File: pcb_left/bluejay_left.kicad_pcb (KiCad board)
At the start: 2 copper layers, 147 x 140.5 mm, 82 parts, among them J1 SJ-43514, U1 ATmega328P-PU, Y1 16MHz

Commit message: remove mounting hole 9
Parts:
- removed H9: M2, MountingHole:MountingHole_2.2mm_M2_Pad
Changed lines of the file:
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@@
     )
-  )
-  (footprint "MountingHole:MountingHole_2.2mm_M2_Pad" (layer "F.Cu")
-    (at 56.95 64.15)
-    (descr "Mounting Hole 2.2mm, M2")
-    (tags "mounting hole 2.2mm m2")
-    (property "Sheetfile" "bluejay_left.kicad_sch")
-    (property "Sheetname" "")
-    (property "exclude_from_bom" "")
-    (attr exclude_from_pos_files exclude_from_bom)
-    (fp_text reference "H9" (at 0 -3.2) (layer "F.SilkS") hide
-      (effects (font (size 1 1) (thickness 0.15)))
-    )
-    (fp_text value "M2" (at 0 3.2) (layer "F.Fab")
-      (effects (font (size 1 1) (thickness 0.15)))
-    )
-    (fp_text user "${REFERENCE}" (at 0 0) (layer "F.Fab")
-      (effects (font (size 1 1) (thickness 0.15)))
-    )
-    (fp_circle (center 0 0) (end 2.2 0) (layer "Cmts.User") (width 0.15) (fill none))
-    (fp_circle (center 0 0) (end 2.45 0) (layer "F.CrtYd") (width 0.05) (fill none))
-    (pad "1" thru_hole circle (at 0 0) (size 4.4 4.4) (drill 2.2) (layers *.Cu *.Mask))
   )
   (footprint "BlueJay footprints:SW_MX_Plate" (layer "F.Cu")

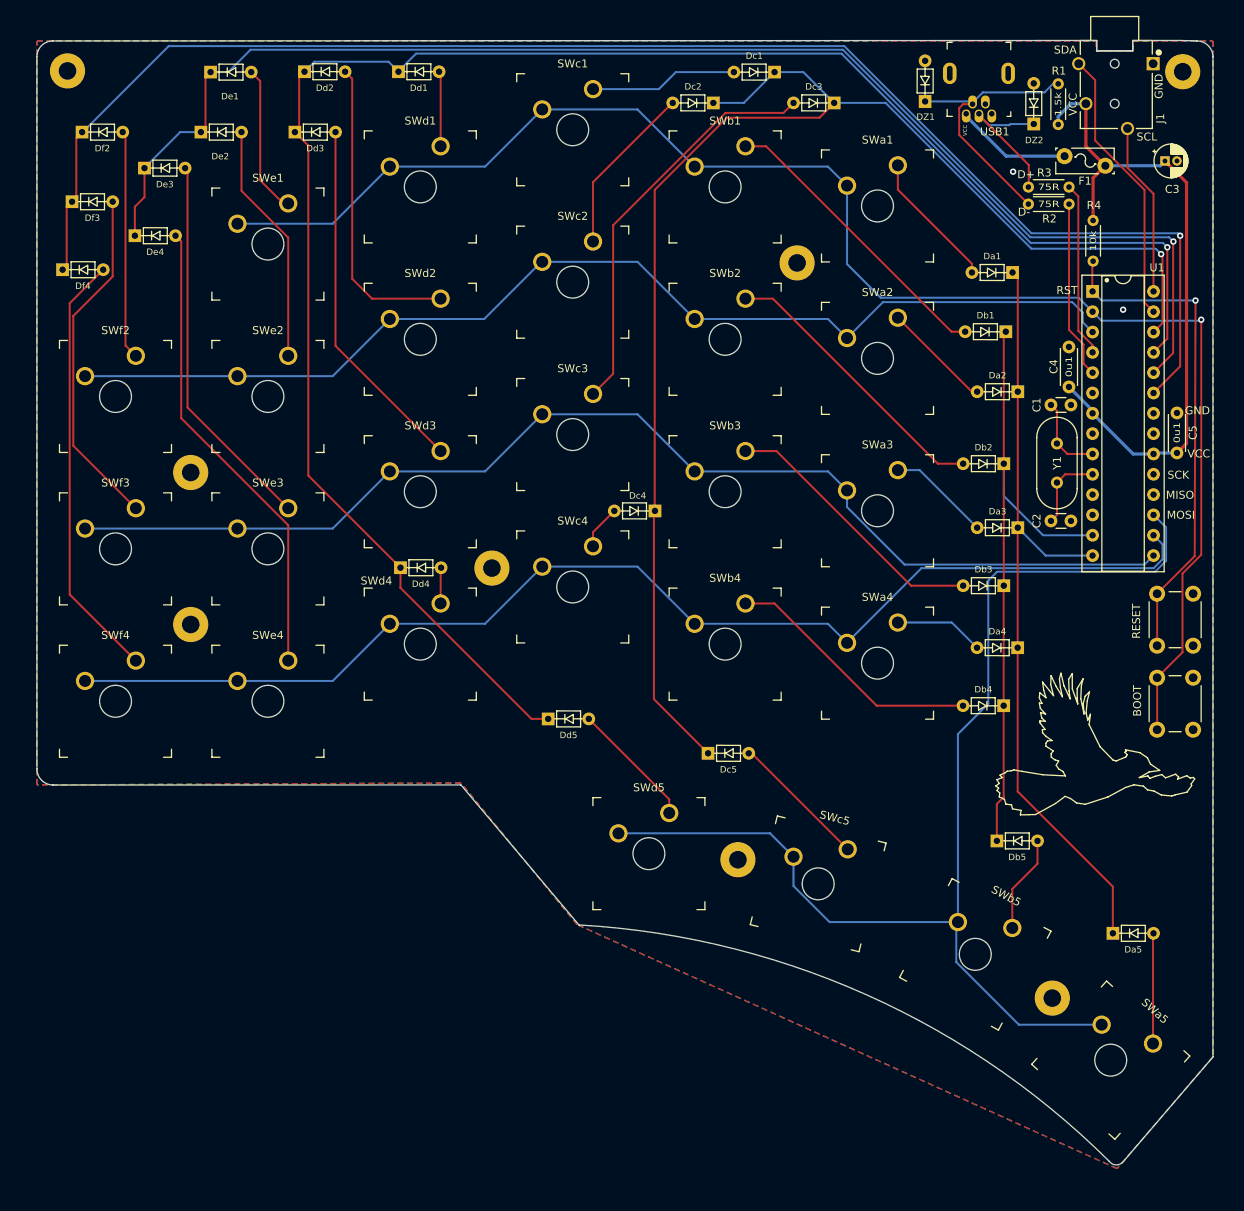
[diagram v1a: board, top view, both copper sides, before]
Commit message: Round edges of PCB
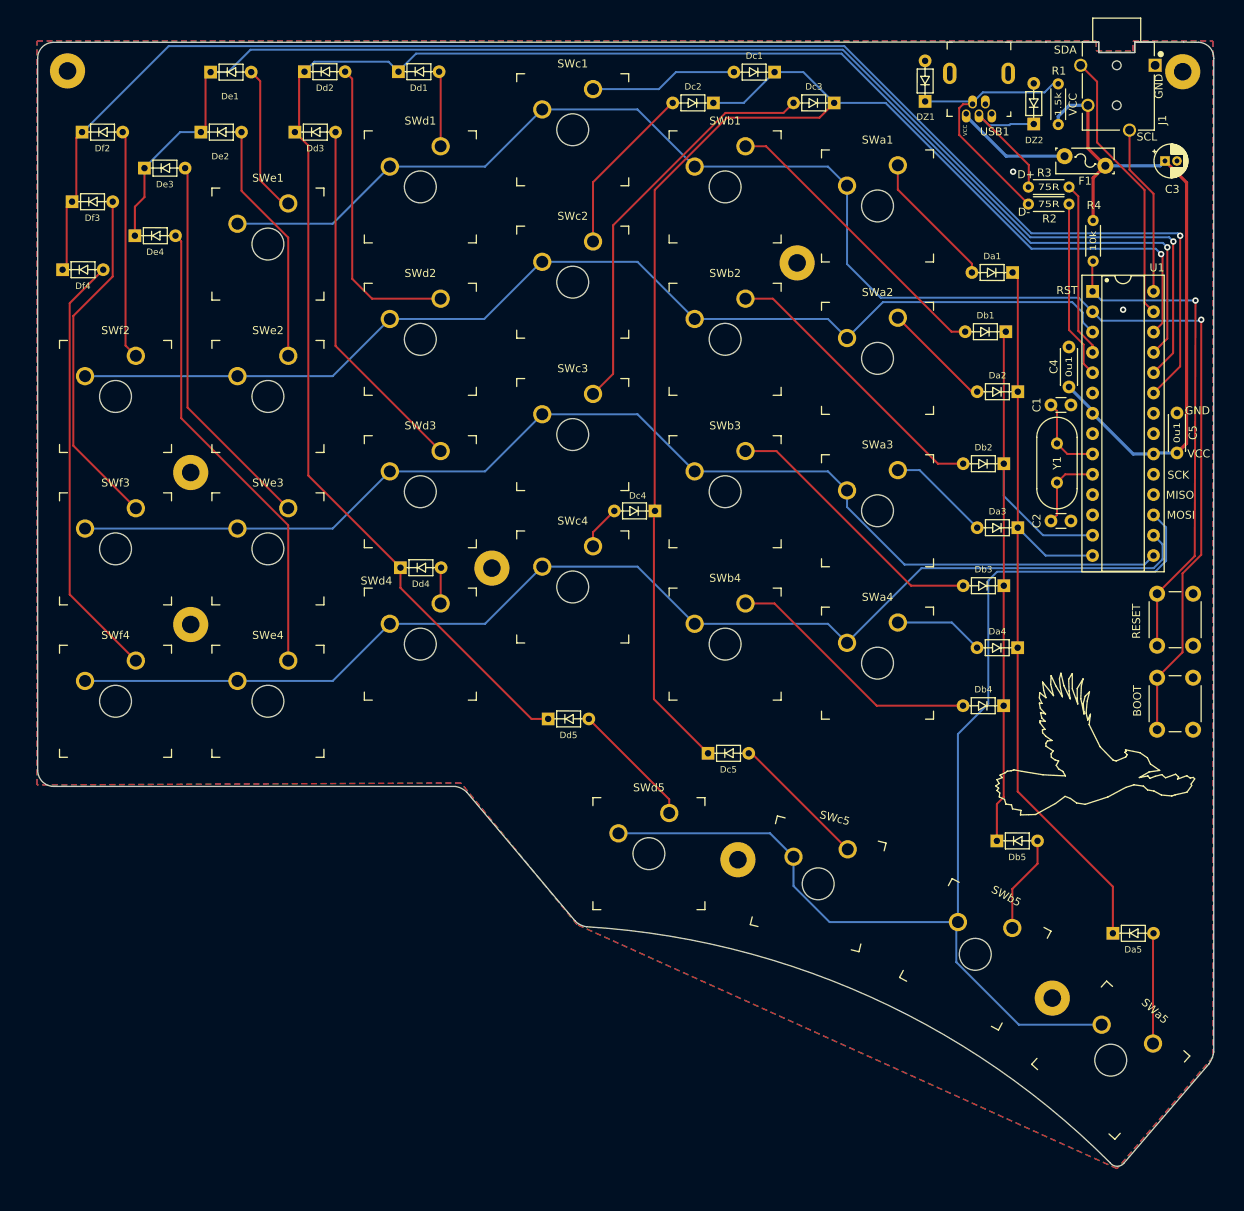
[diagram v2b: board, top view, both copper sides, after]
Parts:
- moved J1 0.32 mm to (49.0, -50.7)
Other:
- outline, holes or cut-outs redrawn
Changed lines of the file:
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@@
   )
   (footprint "BlueJay footprints:CUI_SJ-43514" (layer "F.Cu")
-    (at 48.7 -50.9 -90)
+    (at 48.95 -50.7 -90)
     (property "Field4" "MANUFACTURER RECOMMENDATIONS")
     (property "Field5" "CUI INC")
@@
   (gr_line locked (start 26.028999 -42.674998) (end 26.028999 -42.674998) (layer "Eco1.User") (width 0.188976))
   (gr_line locked (start -16.546013 52.286989) (end -16.546013 38.286989) (layer "Eco1.User") (width 0.188976))
-  (gr_line (start 60.9812 70.6563) (end 49.7812 83.7263) (layer "Edge.Cuts") (width 0.1))
-  (gr_arc (start -18.2688 54.1563) (mid 17.583107 62.841492) (end 48.0112 83.6963) (layer "Edge.Cuts") (width 0.1))
-  (gr_arc (start 58.9812 -56.3437) (mid 60.393459 -55.755959) (end 60.981199 -54.3437) (layer "Edge.Cuts") (width 0.1))
-  (gr_line (start 60.9812 70.6563) (end 60.981199 -54.3437) (layer "Edge.Cuts") (width 0.1))
-  (gr_arc (start -86.024489 -54.35145) (mid -85.442713 -55.767431) (end -84.024489 -56.3437) (layer "Edge.Cuts") (width 0.1))
-  (gr_arc (start -84.02552 36.663017) (mid -85.443204 36.061839) (end -86.025519 34.6363) (layer "Edge.Cuts") (width 0.1))
-  (gr_line (start -86.024489 -54.35145) (end -86.025519 34.6363) (layer "Edge.Cuts") (width 0.1))
-  (gr_line (start -84.02552 36.663017) (end -33.0188 36.6563) (layer "Edge.Cuts") (width 0.1))
-  (gr_line (start -33.0188 36.6563) (end -18.2688 54.1563) (layer "Edge.Cuts") (width 0.1))
-  (gr_line (start 58.9812 -56.3437) (end 57.05 -56.4) (layer "Edge.Cuts") (width 0.1))
-  (gr_line (start 39.85 -56.4) (end -84.024489 -56.3437) (layer "Edge.Cuts") (width 0.1))
-  (gr_arc (start 49.7812 83.7263) (mid 48.888799 84.147698) (end 48.0112 83.6963) (layer "Edge.Cuts") (width 0.1))
+  (gr_line (start 60.48 71.53) (end 49.88 83.9) (layer "Edge.Cuts") (width 0.1))
+  (gr_arc (start -17.32 54.38) (mid 18.101214 63.120674) (end 48.11 83.87) (layer "Edge.Cuts") (width 0.1))
+  (gr_arc (start 59.2 -56.175) (mid 60.553201 -55.55994) (end 61.08 -54.17) (layer "Edge.Cuts") (width 0.1))
+  (gr_line (start 61.08 70.05) (end 61.08 -54.17) (layer "Edge.Cuts") (width 0.1))
+  (gr_arc (start -85.93 -54.18) (mid -85.347749 -55.594848) (end -83.93 -56.17) (layer "Edge.Cuts") (width 0.1))
+  (gr_arc (start -83.93 36.84) (mid -85.348353 36.23717) (end -85.93 34.81) (layer "Edge.Cuts") (width 0.1))
+  (gr_line (start -85.93 -54.18) (end -85.93 34.81) (layer "Edge.Cuts") (width 0.1))
+  (gr_line (start -83.93 36.84) (end -33.72 36.84) (layer "Edge.Cuts") (width 0.1))
+  (gr_line (start -32.31 37.54) (end -18.73 53.68) (layer "Edge.Cuts") (width 0.1))
+  (gr_line (start 59.2 -56.175) (end 57.3 -56.2) (layer "Edge.Cuts") (width 0.1))
+  (gr_arc (start -17.32 54.38) (mid -18.079496 54.13977) (end -18.73 53.68) (layer "Edge.Cuts") (width 0.1))
+  (gr_arc (start 61.08 70.05) (mid 60.863331 70.823783) (end 60.48 71.53) (layer "Edge.Cuts") (width 0.1))
+  (gr_line (start 40.1 -56.2) (end -83.93 -56.17) (layer "Edge.Cuts") (width 0.1))
+  (gr_arc (start 49.88 83.9) (mid 48.987603 84.321434) (end 48.11 83.87) (layer "Edge.Cuts") (width 0.1))
+  (gr_arc (start -33.72 36.84) (mid -32.960504 37.08023) (end -32.31 37.54) (layer "Edge.Cuts") (width 0.1))
   (gr_text "JLCJLCJLCJLC" (at -80.15 35.09) (layer "B.SilkS")
     (effects (font (size 1 1) (thickness 0.15)) (justify mirror))
@@
   (segment (start 41.4812 -1.1437) (end 41.4812 2.9063) (width 0.25) (layer "F.Cu") (net 3))
   (segment (start 42.515 -2.1775) (end 45.9312 -2.1775) (width 0.25) (layer "F.Cu") (net 3))
-  (segment (start 45.1 -43.1749) (end 45.1 -48.5) (width 0.4) (layer "F.Cu") (net 4))
   (segment (start 57.680711 -38.644189) (end 57.680711 -6.043211) (width 0.4) (layer "F.Cu") (net 4))
   (segment (start 54.9812 -41.3437) (end 57.680711 -38.644189) (width 0.4) (layer "F.Cu") (net 4))
+  (segment (start 45.35 -42.9249) (end 45.35 -48.25) (width 0.4) (layer "F.Cu") (net 4))
   (segment (start 57.680711 -6.043211) (end 56.4812 -4.8437) (width 0.4) (layer "F.Cu") (net 4))
   (segment (start 46 -39.2125) (end 46 -33.9) (width 0.4) (layer "F.Cu") (net 4))
   (segment (start 47.5312 -40.7437) (end 46 -39.2125) (width 0.4) (layer "F.Cu") (net 4))
-  (segment (start 47.5312 -40.7437) (end 45.1 -43.1749) (width 0.4) (layer "F.Cu") (net 4))
+  (segment (start 47.5312 -40.7437) (end 45.35 -42.9249) (width 0.4) (layer "F.Cu") (net 4))
   (segment (start 56.4812 -4.8437) (end 53.6774 -4.8437) (width 0.4) (layer "B.Cu") (net 4))
   (segment (start 54.3812 -40.7437) (end 54.9812 -41.3437) (width 0.4) (layer "B.Cu") (net 4))
   (segment (start 53.6774 -4.8437) (end 53.5512 -4.7175) (width 0.4) (layer "B.Cu") (net 4))
   (segment (start 47.5312 -40.7437) (end 54.3812 -40.7437) (width 0.4) (layer "B.Cu") (net 4))
-  (segment (start 43.23 -48.5) (end 41.64 -46.91) (width 0.4) (layer "B.Cu") (net 4))
+  (segment (start 45.35 -48.3) (end 43.03 -48.3) (width 0.4) (layer "B.Cu") (net 4))
+  (segment (start 41.64 -46.91) (end 41.64 -45.9) (width 0.4) (layer "B.Cu") (net 4))
+  (segment (start 43.03 -48.3) (end 41.64 -46.91) (width 0.4) (layer "B.Cu") (net 4))
   (segment (start 51.0112 -4.7175) (end 45.9312 -9.7975) (width 0.4) (layer "B.Cu") (net 4))
   (segment (start 45.9312 -10.1437) (end 42.9812 -13.0937) (width 0.4) (layer "B.Cu") (net 4))
-  (segment (start 45.1 -48.5) (end 43.23 -48.5) (width 0.4) (layer "B.Cu") (net 4))
   (segment (start 45.9312 -9.7975) (end 45.9312 -10.1437) (width 0.4) (layer "B.Cu") (net 4))
-  (segment (start 41.64 -46.91) (end 41.64 -45.9) (width 0.4) (layer "B.Cu") (net 4))
   (segment (start 53.5512 -4.7175) (end 51.0112 -4.7175) (width 0.4) (layer "B.Cu") (net 4))
   (segment (start 36.5863 -26.7437) (end 35.93 -27.4) (width 0.25) (layer "F.Cu") (net 5))
@@
   (segment (start 35.138376 -41.9437) (end 42.4312 -41.9437) (width 0.4) (layer "B.Cu") (net 40))
   (segment (start 30.1312 -46.950876) (end 35.138376 -41.9437) (width 0.4) (layer "B.Cu") (net 40))
-  (segment (start 50.3 -45.4) (end 50.3 -40.490832) (width 0.25) (layer "F.Cu") (net 41))
+  (segment (start 50.55 -45.15) (end 50.55 -40.240832) (width 0.25) (layer "F.Cu") (net 41))
   (segment (start 53.5512 -37.239632) (end 53.5512 -25.0375) (width 0.25) (layer "F.Cu") (net 41))
-  (segment (start 50.3 -40.490832) (end 53.5512 -37.239632) (width 0.25) (layer "F.Cu") (net 41))
-  (segment (start 44.2 -53.5) (end 46.249511 -51.450489) (width 0.25) (layer "F.Cu") (net 42))
-  (segment (start 46.249511 -51.450489) (end 46.249511 -43.905603) (width 0.25) (layer "F.Cu") (net 42))
+  (segment (start 50.55 -40.240832) (end 53.5512 -37.239632) (width 0.25) (layer "F.Cu") (net 41))
+  (segment (start 44.45 -53.3) (end 46.499511 -51.250489) (width 0.25) (layer "F.Cu") (net 42))
+  (segment (start 46.499511 -51.250489) (end 46.499511 -43.655603) (width 0.25) (layer "F.Cu") (net 42))
+  (segment (start 46.499511 -43.655603) (end 52.426689 -37.728425) (width 0.25) (layer "F.Cu") (net 42))
   (segment (start 52.426689 -37.728425) (end 52.426689 -23.622011) (width 0.25) (layer "F.Cu") (net 42))
-  (segment (start 46.249511 -43.905603) (end 52.426689 -37.728425) (width 0.25) (layer "F.Cu") (net 42))
   (segment (start 52.426689 -23.622011) (end 53.5512 -22.4975) (width 0.25) (layer "F.Cu") (net 42))
   (segment (start 45.9 -25.0687) (end 45.9312 -25.0375) (width 0.25) (layer "F.Cu") (net 43))

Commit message: tweak board edges
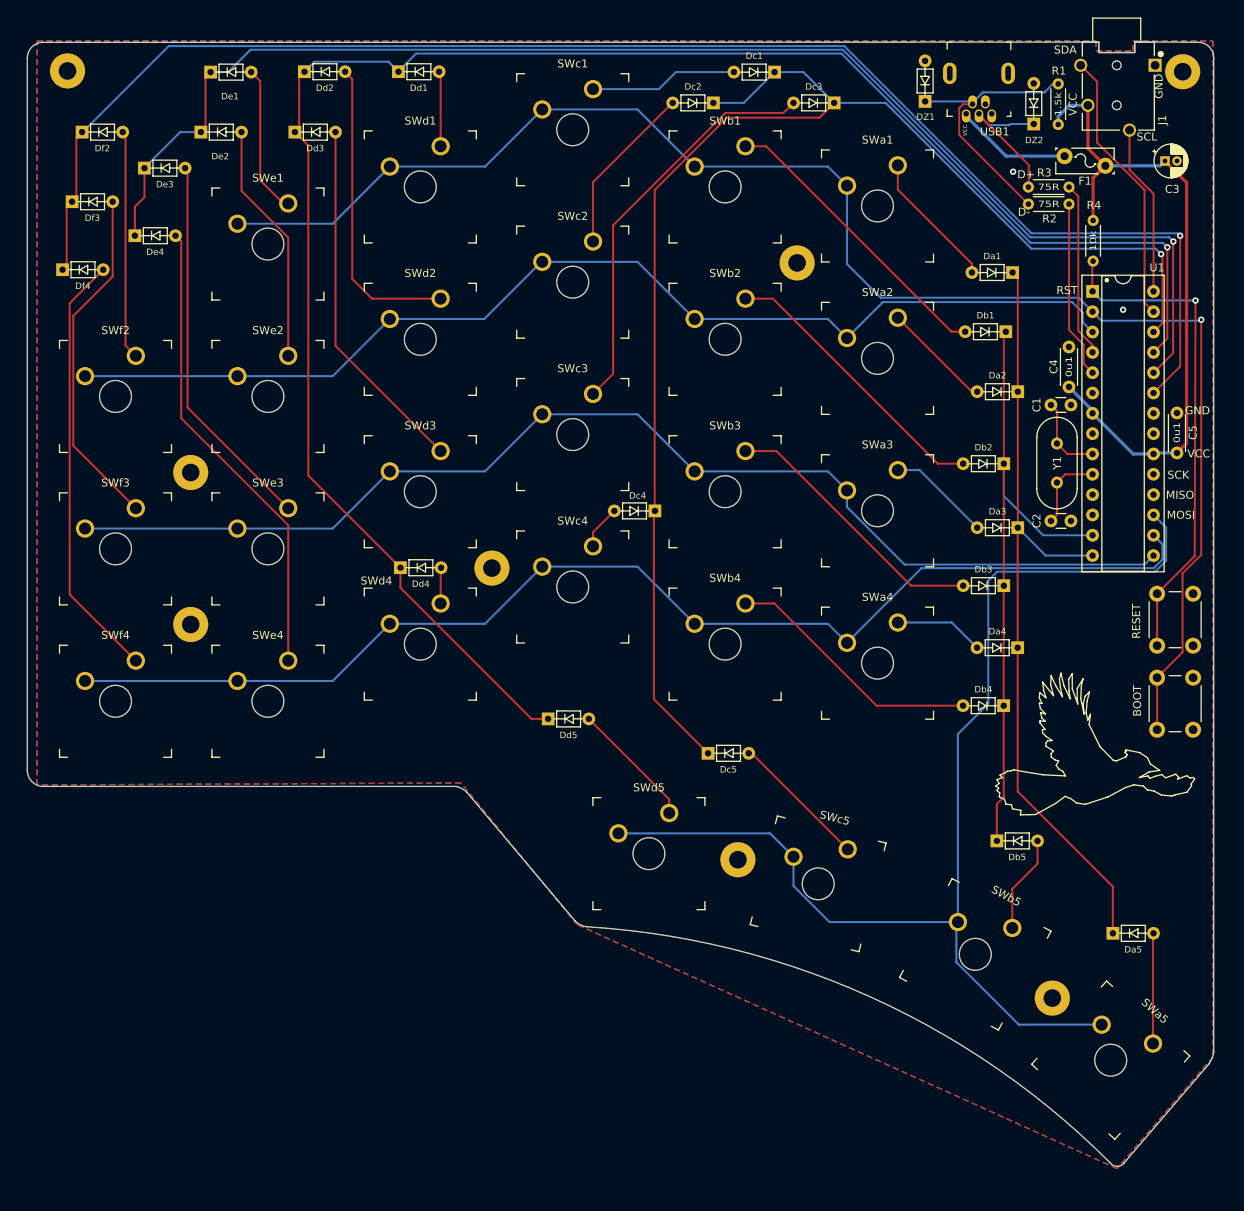
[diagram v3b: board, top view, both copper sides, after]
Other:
- board size 147 x 140.5 mm -> 148.3 x 140.5 mm
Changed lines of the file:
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@@
   (gr_arc (start 59.2 -56.175) (mid 60.553201 -55.55994) (end 61.08 -54.17) (layer "Edge.Cuts") (width 0.1))
   (gr_line (start 61.08 70.05) (end 61.08 -54.17) (layer "Edge.Cuts") (width 0.1))
-  (gr_arc (start -85.93 -54.18) (mid -85.347749 -55.594848) (end -83.93 -56.17) (layer "Edge.Cuts") (width 0.1))
-  (gr_arc (start -83.93 36.84) (mid -85.348353 36.23717) (end -85.93 34.81) (layer "Edge.Cuts") (width 0.1))
-  (gr_line (start -85.93 -54.18) (end -85.93 34.81) (layer "Edge.Cuts") (width 0.1))
-  (gr_line (start -83.93 36.84) (end -33.72 36.84) (layer "Edge.Cuts") (width 0.1))
+  (gr_arc (start -87.23 -54.18) (mid -86.647749 -55.594848) (end -85.23 -56.17) (layer "Edge.Cuts") (width 0.1))
+  (gr_arc (start -85.23 36.84) (mid -86.648353 36.23717) (end -87.23 34.81) (layer "Edge.Cuts") (width 0.1))
+  (gr_line (start -87.23 -54.18) (end -87.23 34.81) (layer "Edge.Cuts") (width 0.1))
+  (gr_line (start -85.23 36.84) (end -33.72 36.84) (layer "Edge.Cuts") (width 0.1))
   (gr_line (start -32.31 37.54) (end -18.73 53.68) (layer "Edge.Cuts") (width 0.1))
   (gr_line (start 59.2 -56.175) (end 57.3 -56.2) (layer "Edge.Cuts") (width 0.1))
   (gr_arc (start -17.32 54.38) (mid -18.079496 54.13977) (end -18.73 53.68) (layer "Edge.Cuts") (width 0.1))
   (gr_arc (start 61.08 70.05) (mid 60.863331 70.823783) (end 60.48 71.53) (layer "Edge.Cuts") (width 0.1))
-  (gr_line (start 40.1 -56.2) (end -83.93 -56.17) (layer "Edge.Cuts") (width 0.1))
+  (gr_line (start 40.1 -56.2) (end -85.23 -56.17) (layer "Edge.Cuts") (width 0.1))
   (gr_arc (start 49.88 83.9) (mid 48.987603 84.321434) (end 48.11 83.87) (layer "Edge.Cuts") (width 0.1))
   (gr_arc (start -33.72 36.84) (mid -32.960504 37.08023) (end -32.31 37.54) (layer "Edge.Cuts") (width 0.1))
